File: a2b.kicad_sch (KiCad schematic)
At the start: 15 parts, among them SW1 SW_DIP_x02, SW2 SW_DIP_x02, SW3 SW_DIP_x02

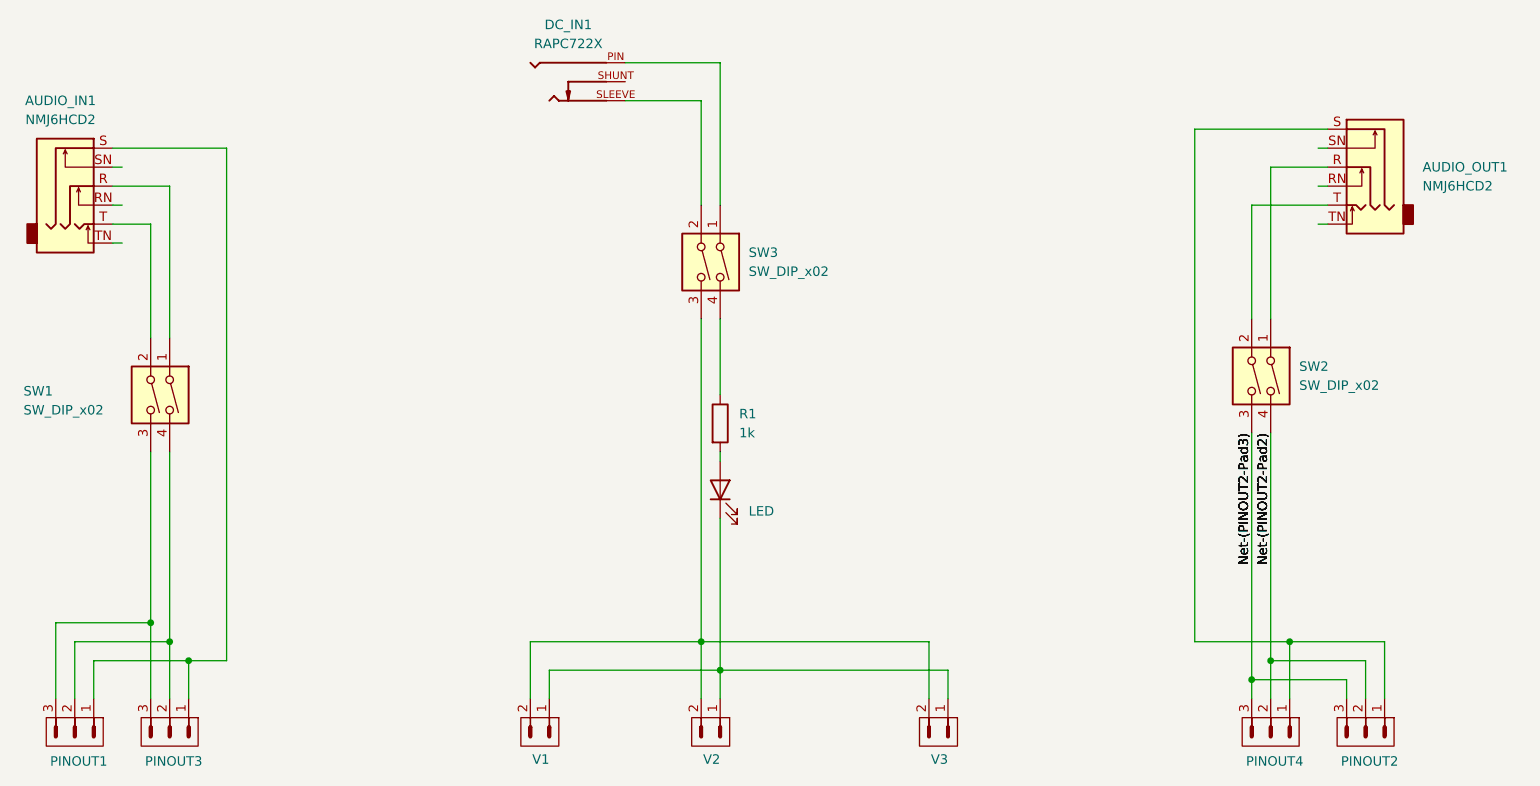
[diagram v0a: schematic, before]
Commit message: Change 2 switch dip switches from 2 switch to 3 switch so you can control the ground.
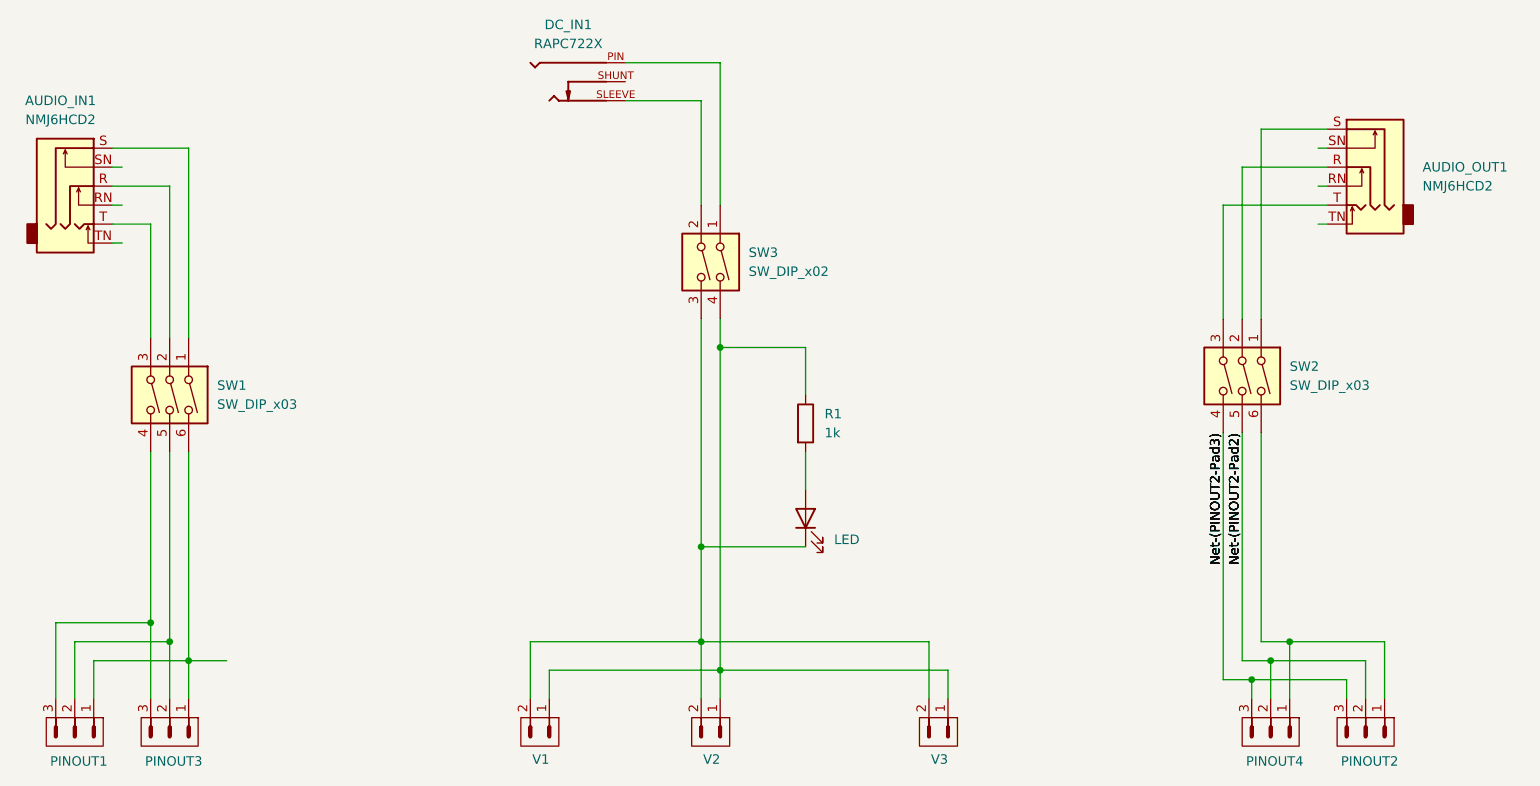
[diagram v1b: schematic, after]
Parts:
- removed SW1, SW2: SW_DIP_x02, Button_Switch_THT:SW_DIP_SPSTx02_Slide_9.78x7.26mm_W7.62mm_P2.54mm, symbol Switch:SW_DIP_x02
- added SW1, SW2: SW_DIP_x03, Button_Switch_THT:SW_DIP_SPSTx03_Slide_9.78x9.8mm_W7.62mm_P2.54mm, symbol Switch:SW_DIP_x03
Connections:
- net Net-(PINOUT2-Pad2): now also SW2.5
- net Net-(PINOUT2-Pad3): now also SW2.4
- net at SW3.3, V1.2, V2.2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: now also D1.1 (K)
- net at R1.1, SW3.4: now also V1.1, V2.1, V3.1
- net at AUDIO_OUT1.R: now also SW2.2
- net at AUDIO_OUT1.T: now also SW2.3
- net at PINOUT2.1, PINOUT4.1: now also SW2.6; no longer AUDIO_OUT1.S
- net at AUDIO_IN1.R: now also SW1.2
- net at PINOUT1.1, PINOUT3.1: now also SW1.6; no longer AUDIO_IN1.S
- net at AUDIO_IN1.T: now also SW1.3
- net at PINOUT1.2, PINOUT3.2: now also SW1.5
- net at PINOUT1.3, PINOUT3.3: now also SW1.4
- new net: AUDIO_OUT1.S, SW2.1
- new net: AUDIO_IN1.S, SW1.1
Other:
- moved on the sheet: R1

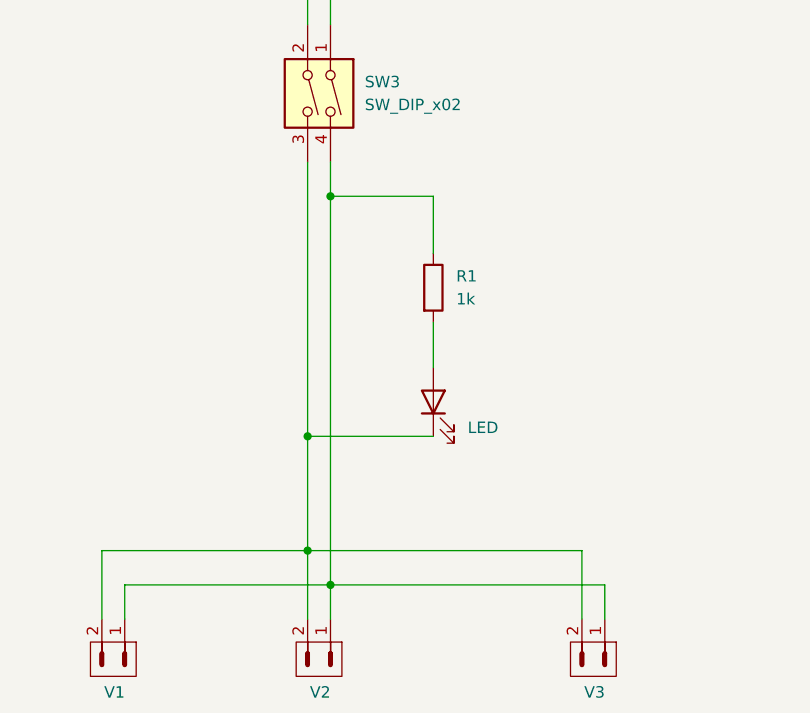
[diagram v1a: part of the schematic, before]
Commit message: Swap + & - on board silkscreen and added extra + & - prongs.
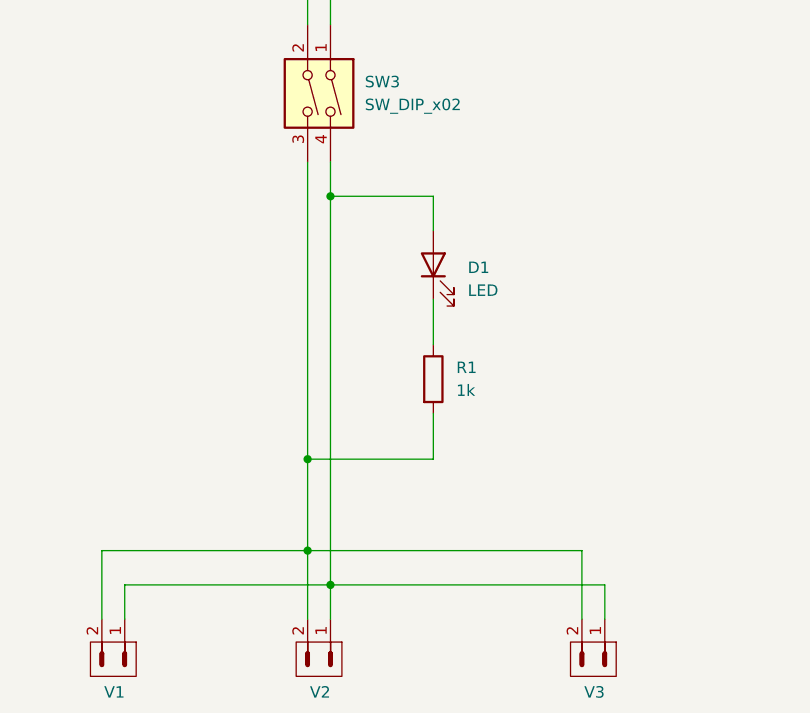
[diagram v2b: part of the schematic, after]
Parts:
- D1: footprint LED_THT:LED_D5.0mm -> (none); KiLib_Generator LED/THT -> (none)
- R1: footprint Resistor_THT:R_Axial_DIN0207_L6.3mm_D2.5mm_P10.16mm_Horizontal -> (none); KiLib_Generator resistor/THT -> (none)
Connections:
- net at SW3.3, V1.2, V2.2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: now also R1.2; no longer D1.1 (K)
- net at SW3.4, V1.1, V2.1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: now also D1.2 (A); no longer R1.1
- new net: D1.1 (K), R1.1
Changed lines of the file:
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@@
+	)
+	(junction
+		(at 144.78 109.22)
+		(diameter 0)
+		(color 0 0 0 0)
 	)
 	(junction
@@
 		(color 0 0 0 0)
 	)
-	(junction
-		(at 144.78 106.68)
-		(diameter 0)
-		(color 0 0 0 0)
-	)
 	(wire
 		(pts
@@
 	(wire
 		(pts
-			(xy 158.75 106.68) (xy 144.78 106.68)
+			(xy 158.75 109.22) (xy 144.78 109.22)
 		)
 		(stroke
@@
 	(wire
 		(pts
+			(xy 158.75 91.44) (xy 158.75 96.52)
+		)
+		(stroke
+			(width 0)
+			(type default)
+		)
+	)
+	(wire
+		(pts
 			(xy 214.63 124.46) (xy 218.44 124.46)
 		)
@@
 	(wire
 		(pts
+			(xy 158.75 109.22) (xy 158.75 104.14)
+		)
+		(stroke
+			(width 0)
+			(type default)
+		)
+	)
+	(wire
+		(pts
 			(xy 158.75 80.01) (xy 147.32 80.01)
 		)
@@
 	(wire
 		(pts
-			(xy 144.78 106.68) (xy 144.78 119.38)
-		)
-		(stroke
-			(width 0)
-			(type default)
-		)
-	)
-	(wire
-		(pts
 			(xy 66.04 66.04) (xy 67.31 66.04)
 		)
@@
 	(wire
 		(pts
-			(xy 158.75 93.98) (xy 158.75 99.06)
-		)
-		(stroke
-			(width 0)
-			(type default)
-		)
-	)
-	(wire
-		(pts
 			(xy 219.71 119.38) (xy 223.52 119.38)
 		)
@@
 	(wire
 		(pts
+			(xy 144.78 109.22) (xy 144.78 119.38)
+		)
+		(stroke
+			(width 0)
+			(type default)
+		)
+	)
+	(wire
+		(pts
 			(xy 134.62 46.99) (xy 144.78 46.99)
 		)
@@
 	(wire
 		(pts
+			(xy 144.78 76.2) (xy 144.78 109.22)
+		)
+		(stroke
+			(width 0)
+			(type default)
+		)
+	)
+	(wire
+		(pts
 			(xy 175.26 119.38) (xy 144.78 119.38)
 		)
@@
 	(wire
 		(pts
-			(xy 144.78 76.2) (xy 144.78 106.68)
-		)
-		(stroke
-			(width 0)
-			(type default)
-		)
-	)
-	(wire
-		(pts
-			(xy 158.75 86.36) (xy 158.75 80.01)
+			(xy 158.75 83.82) (xy 158.75 80.01)
 		)
 		(stroke
@@
 				(path "/2fb67ef4-3b78-48fd-981f-3213cdbc031d"
 					(reference "SW2")
-					(unit 1)
-				)
-			)
-		)
-	)
-	(symbol
-		(lib_id "Device:R")
-		(at 158.75 90.17 0)
-		(unit 1)
-		(body_style 1)
-		(exclude_from_sim no)
-		(in_bom yes)
-		(on_board yes)
-		(in_pos_files yes)
-		(dnp no)
-		(fields_autoplaced yes)
-		(property "Reference" "R1"
-			(at 161.29 88.8999 0)
-			(show_name no)
-			(do_not_autoplace no)
-			(effects
-				(font
-					(size 1.27 1.27)
-				)
-				(justify left)
-			)
-		)
-		(property "Value" "1k"
-			(at 161.29 91.4399 0)
-			(show_name no)
-			(do_not_autoplace no)
-			(effects
-				(font
-					(size 1.27 1.27)
-				)
-				(justify left)
-			)
-		)
-		(property "Footprint" "Resistor_THT:R_Axial_DIN0207_L6.3mm_D2.5mm_P10.16mm_Horizontal"
-			(at 156.972 90.17 90)
-			(hide yes)
-			(show_name no)
-			(do_not_autoplace no)
-			(effects
-				(font
-					(size 1.27 1.27)
-				)
-			)
-		)
-		(property "Datasheet" ""
-			(at 158.75 90.17 0)
-			(hide yes)
-			(show_name no)
-			(do_not_autoplace no)
-			(effects
-				(font
-					(size 1.27 1.27)
-				)
-			)
-		)
-		(property "Description" "Resistor"
-			(at 158.75 90.17 0)
-			(hide yes)
-			(show_name no)
-			(do_not_autoplace no)
-			(effects
-				(font
-					(size 1.27 1.27)
-				)
-			)
-		)
-		(property "KiLib_Generator" "resistor/THT"
-			(at 158.75 90.17 0)
-			(hide yes)
-			(show_name no)
-			(do_not_autoplace no)
-			(effects
-				(font
-					(size 1.27 1.27)
-				)
-			)
-		)
-		(pin "2"
-		)
-		(pin "1"
-		)
-		(instances
-			(project "a2b"
-				(path "/2fb67ef4-3b78-48fd-981f-3213cdbc031d"
-					(reference "R1")
 					(unit 1)
 				)
@@
 	)
 	(symbol
+		(lib_id "Device:R")
+		(at 158.75 100.33 0)
+		(unit 1)
+		(body_style 1)
+		(exclude_from_sim no)
+		(in_bom yes)
+		(on_board yes)
+		(in_pos_files yes)
+		(dnp no)
+		(fields_autoplaced yes)
+		(property "Reference" "R1"
+			(at 161.29 99.0599 0)
+			(show_name no)
+			(do_not_autoplace no)
+			(effects
+				(font
+					(size 1.27 1.27)
+				)
+				(justify left)
+			)
+		)
+		(property "Value" "1k"
+			(at 161.29 101.5999 0)
+			(show_name no)
+			(do_not_autoplace no)
+			(effects
+				(font
+					(size 1.27 1.27)
+				)
+				(justify left)
+			)
+		)
+		(property "Footprint" ""
+			(at 156.972 100.33 90)
+			(hide yes)
+			(show_name no)
+			(do_not_autoplace no)
+			(effects
+				(font
+					(size 1.27 1.27)
+				)
+			)
+		)
+		(property "Datasheet" ""
+			(at 158.75 100.33 0)
+			(hide yes)
+			(show_name no)
+			(do_not_autoplace no)
+			(effects
+				(font
+					(size 1.27 1.27)
+				)
+			)
+		)
+		(property "Description" "Resistor"
+			(at 158.75 100.33 0)
+			(hide yes)
+			(show_name no)
+			(do_not_autoplace no)
+			(effects
+				(font
+					(size 1.27 1.27)
+				)
+			)
+		)
+		(pin "1"
+		)
+		(pin "2"
+		)
+		(instances
+			(project "a2b"
+				(path "/2fb67ef4-3b78-48fd-981f-3213cdbc031d"
+					(reference "R1")
+					(unit 1)
+				)
+			)
+		)
+	)
+	(symbol
 		(lib_id "Device:LED")
-		(at 158.75 102.87 90)
+		(at 158.75 87.63 90)
 		(unit 1)
 		(body_style 1)
@@
 		(fields_autoplaced yes)
 		(property "Reference" "D1"
-			(at 162.56 103.1874 90)
-			(hide yes)
+			(at 162.56 87.9474 90)
 			(show_name no)
 			(do_not_autoplace no)
@@
 		)
 		(property "Value" "LED"
-			(at 162.56 105.7274 90)
+			(at 162.56 90.4874 90)
 			(show_name no)
 			(do_not_autoplace no)
@@
 			)
 		)
-		(property "Footprint" "LED_THT:LED_D5.0mm"
-			(at 158.75 102.87 0)
+		(property "Footprint" ""
+			(at 158.75 87.63 0)
 			(hide yes)
 			(show_name no)
@@
 		)
 		(property "Datasheet" ""
-			(at 158.75 102.87 0)
+			(at 158.75 87.63 0)
 			(hide yes)
 			(show_name no)
@@
 		)
 		(property "Description" "Light emitting diode"
-			(at 158.75 102.87 0)
+			(at 158.75 87.63 0)
 			(hide yes)
 			(show_name no)
@@
 		)
 		(property "Sim.Pins" "1=K 2=A"
-			(at 158.75 102.87 0)
-			(hide yes)
-			(show_name no)
-			(do_not_autoplace no)
-			(effects
-				(font
-					(size 1.27 1.27)
-				)
-			)
-		)
-		(property "KiLib_Generator" "LED/THT"
-			(at 158.75 102.87 0)
-			(hide yes)
-			(show_name no)
+			(at 158.75 87.63 0)
+			(hide yes)
+			(show_name no)

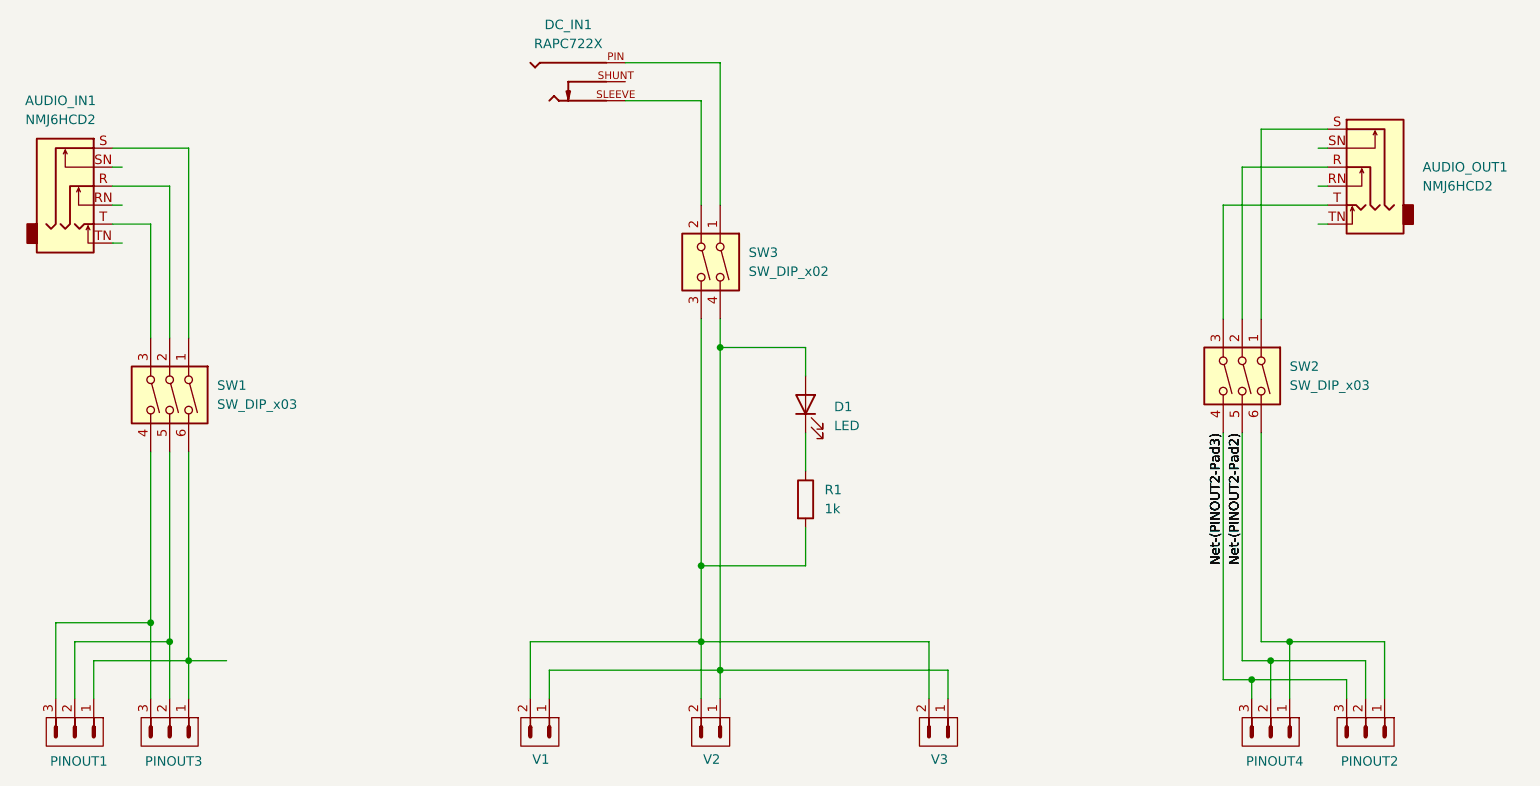
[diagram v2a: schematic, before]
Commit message: update pcb components and routing
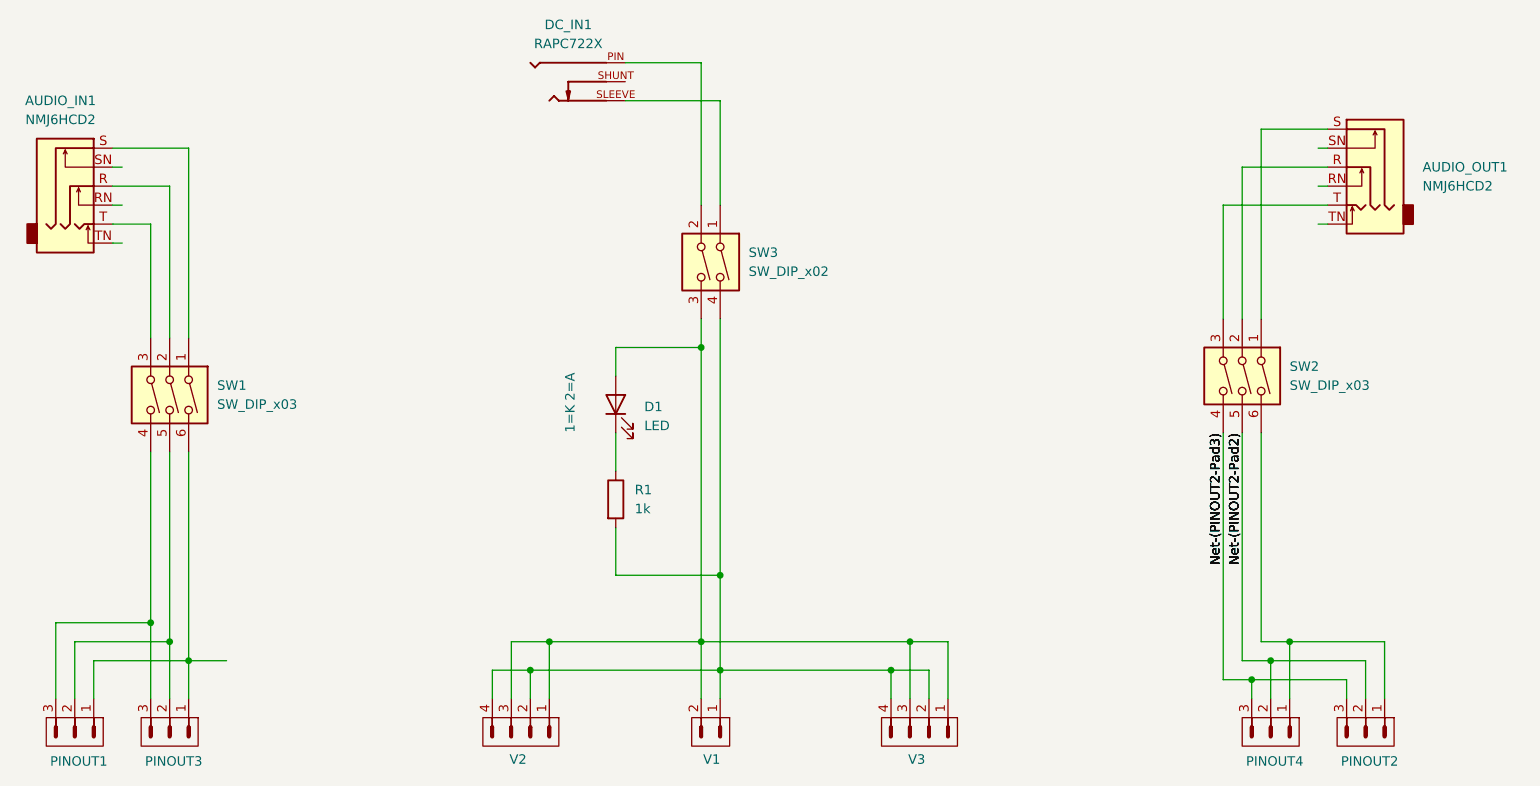
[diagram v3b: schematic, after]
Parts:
- removed V1: (no value), Connector_PinHeader_2.54mm:PinHeader_1x02_P2.54mm_Vertical, symbol customHeaders:2pinHeader
- added V2: (no value), Connector_PinHeader_2.54mm:PinHeader_2x02_P2.54mm_Vertical, symbol customHeaders:2pinHeader
- D1: footprint (none) -> LED_THT:LED_D5.0mm
- R1: footprint (none) -> Resistor_THT:R_Axial_DIN0207_L6.3mm_D2.5mm_P10.16mm_Horizontal
- V3: footprint Connector_PinHeader_2.54mm:PinHeader_1x02_P2.54mm_Vertical -> Connector_PinHeader_2.54mm:PinHeader_2x02_P2.54mm_Vertical
- renumbered V2 to V1
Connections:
- net at SW3.1: now also DC_IN1.SLEEVE; no longer DC_IN1.PIN
- net at SW3.2: now also DC_IN1.PIN; no longer DC_IN1.SLEEVE
- net at SW3.3, V1.2: now also D1.2 (A), V3.1, V3.3, V2.1, V2.3; no longer R1.2, V3.2
- net at SW3.4, V1.1: now also R1.2, V3.2, V3.4, V2.2, V2.4; no longer D1.2 (A), V3.1
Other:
- title: (none) -> A2B
